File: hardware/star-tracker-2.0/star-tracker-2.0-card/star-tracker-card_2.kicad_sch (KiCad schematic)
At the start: 88 parts, among them Q1 DMP2240UDM, Q2 DMN3028LQ-7, Q3 DMP3050LVT-7, Q4 DMP3050LVT-7, Q5 DMN3028LQ-7, U1 MAX7310ATE, U2 MIC842LYC5, U3 MIC842LYC5, U4 TPS62112, U5 TS5A21366DCUR, U6 MAX4211FETE

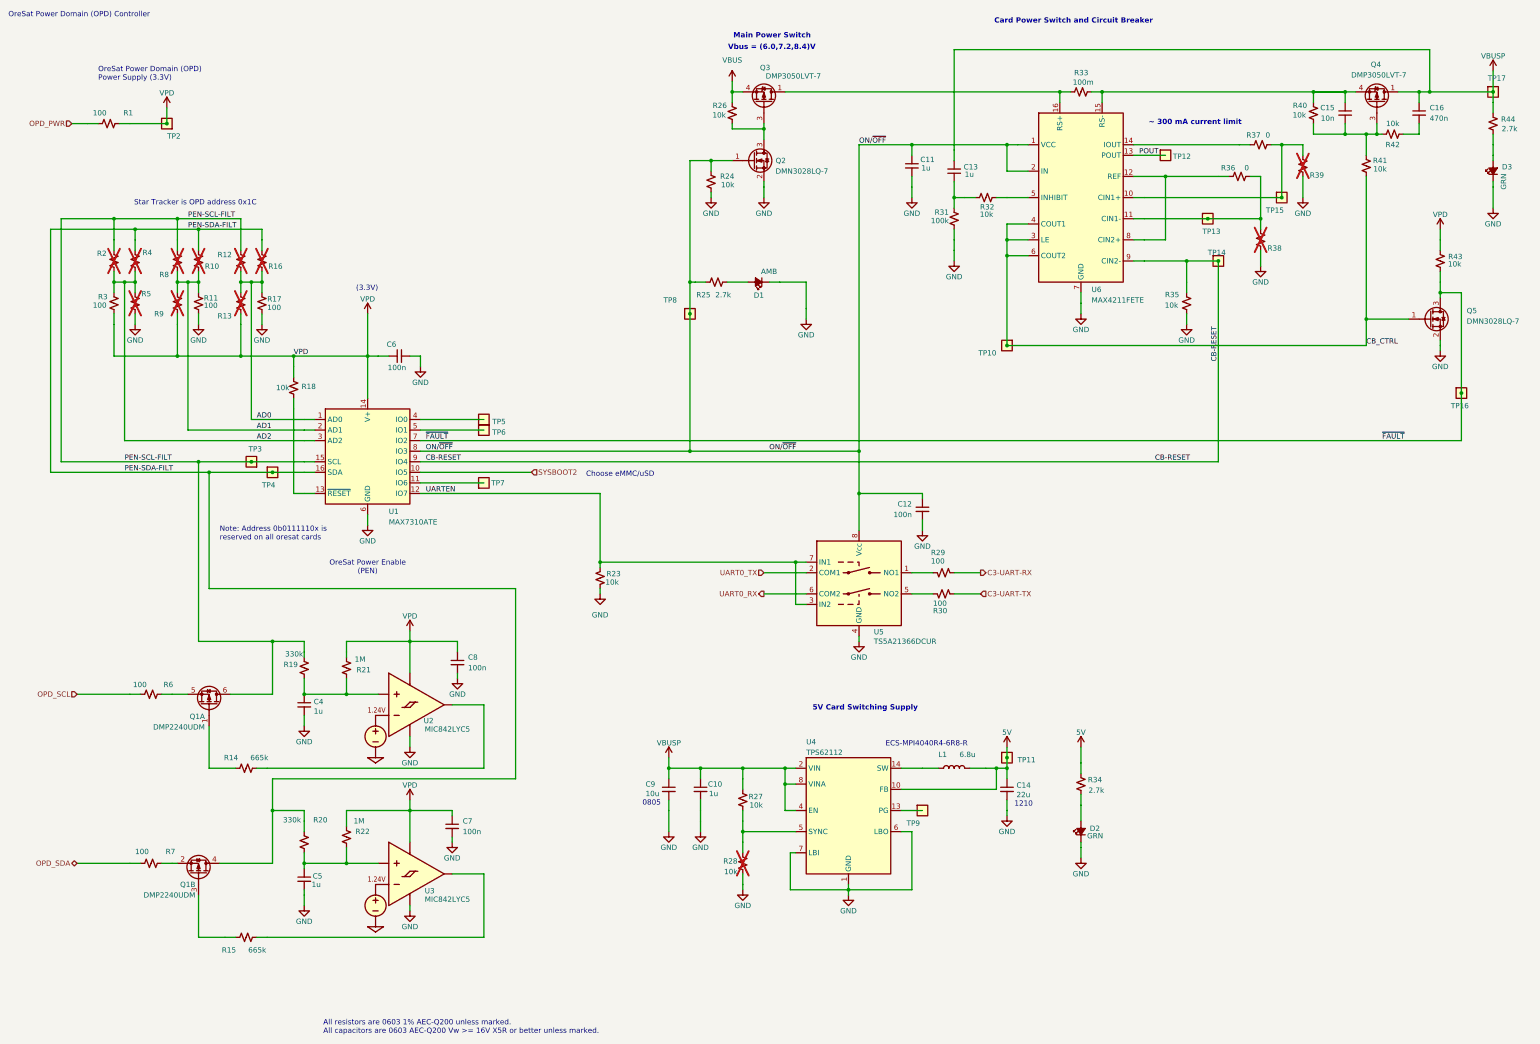
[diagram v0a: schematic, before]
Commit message: Updated USB clamp
minor routing and schematic changes. Updated OPD with new transistors. Changed resistor values on LEDs.
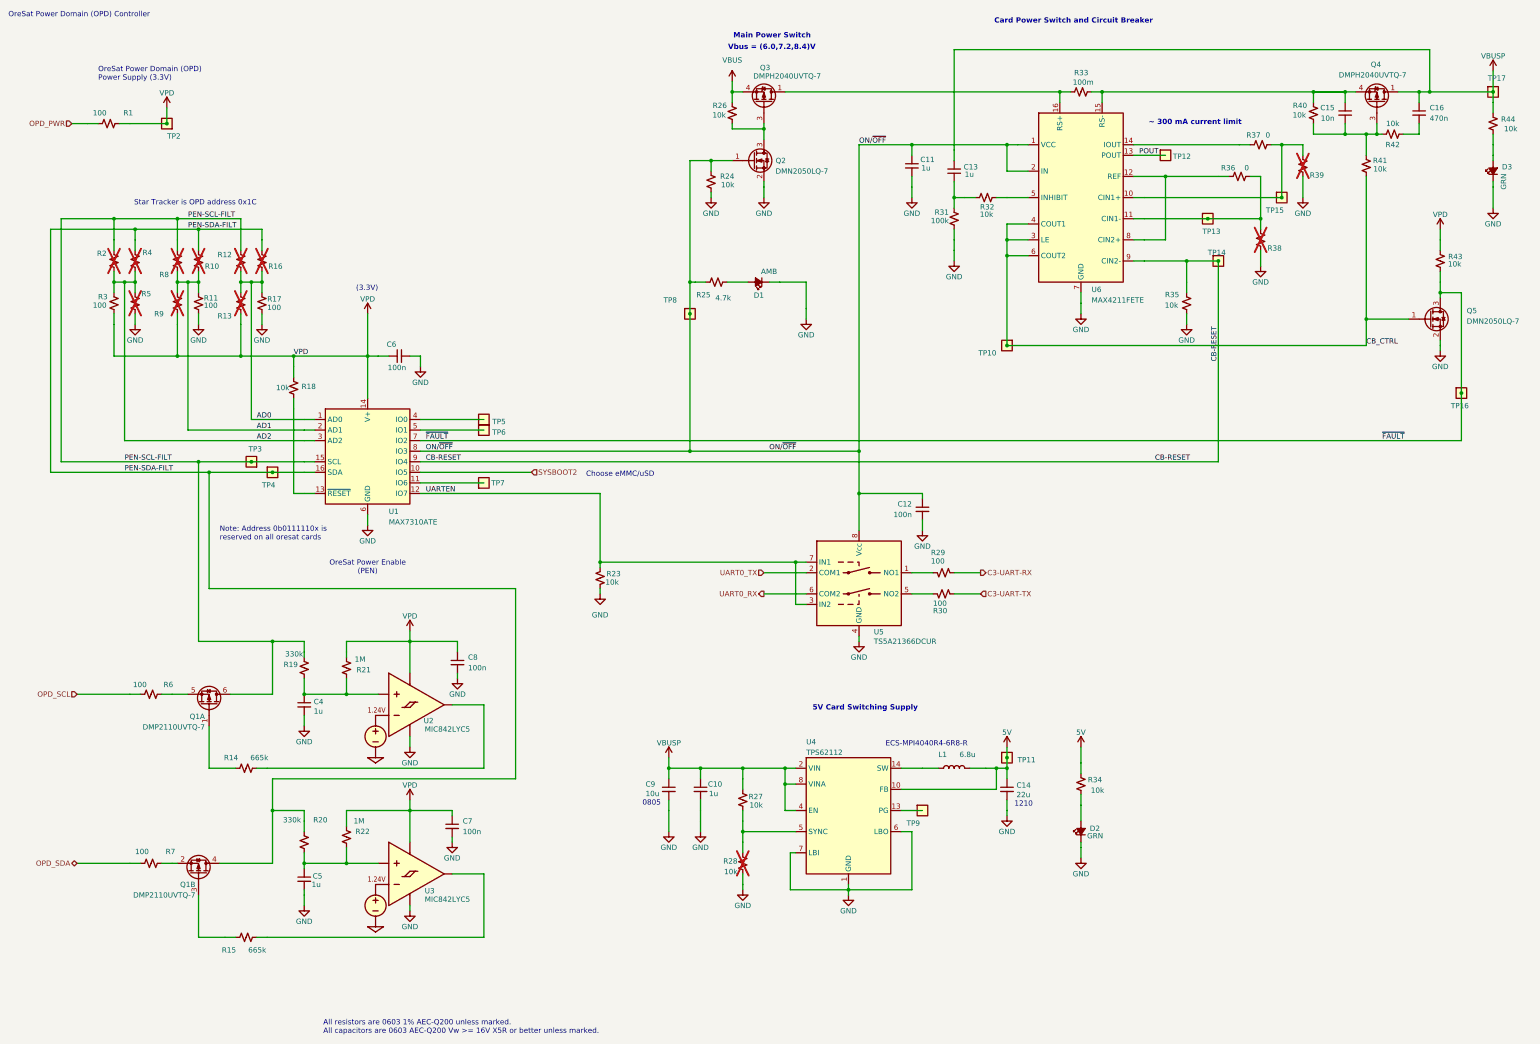
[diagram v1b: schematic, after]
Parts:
- Q1: value DMP2240UDM -> DMP2110UVTQ-7; footprint Package_TO_SOT_SMD:TSOT-23-6 -> Package_TO_SOT_SMD:SOT-23-6; DPN DMP2240UDMDICT-ND -> 31-DMP2110UVTQ-7CT-ND; MFR Diodes Inc -> Diodes Incorporated; MPN DMP2240UDM-7 -> DMP2110UVTQ-7
- Q2, Q5: value DMN3028LQ-7 -> DMN2050LQ-7; footprint Package_TO_SOT_SMD:SOT-23-3 -> Package_TO_SOT_SMD:SOT-23; DPN 31-DMN3028LQ-7CT-ND -> 31-DMN2050LQ-7CT-ND; MPN DMN3028LQ-7 -> DMN2050LQ-7
- Q3, Q4: value DMP3050LVT-7 -> DMPH2040UVTQ-7; DPN 31-DMP3050LVTQ-7-ND -> 31-DMPH2040UVTQ-7CT-ND; MFR Diodes Inc -> Diodes Incorporated; MPN DMP3050LVTQ-7 -> DMPH2040UVTQ-7
- R25: value 2.7k -> 4.7k; DPN RMCF0603FT2K70CT-ND -> RMCF0603FT4K70CT-ND; MPN RMCF0603FT2K70 -> RMCF0603FT4K70
- R34, R44: value 2.7k -> 10k; DPN RMCF0603FT2K70CT-ND -> RMCF0603FT10K0CT-ND; MPN RMCF0603FT2K70 -> RMCF0603FT10K0
